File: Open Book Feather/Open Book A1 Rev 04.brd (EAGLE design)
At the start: 77.5 x 112.3 mm, 125 parts, among them J1 SJ-43514-SMT, J2 10118193-0001LF, Q1 DMG341, Q2 IRLML0100, SW1 SPDT_SWITCH, U1 AP2112-3.3, U2 MCP73831T-2ACI/OT, U3 ATSAMD51J64-TQFP(10X10), U4 GD25Q16C (or GD25Q32C), U5 74AC165D, U6 GD25Q16C (or GD25Q32C), U7 MAX4468EKAT, X1 JSTPH, X2 2x5 0.05" SWD

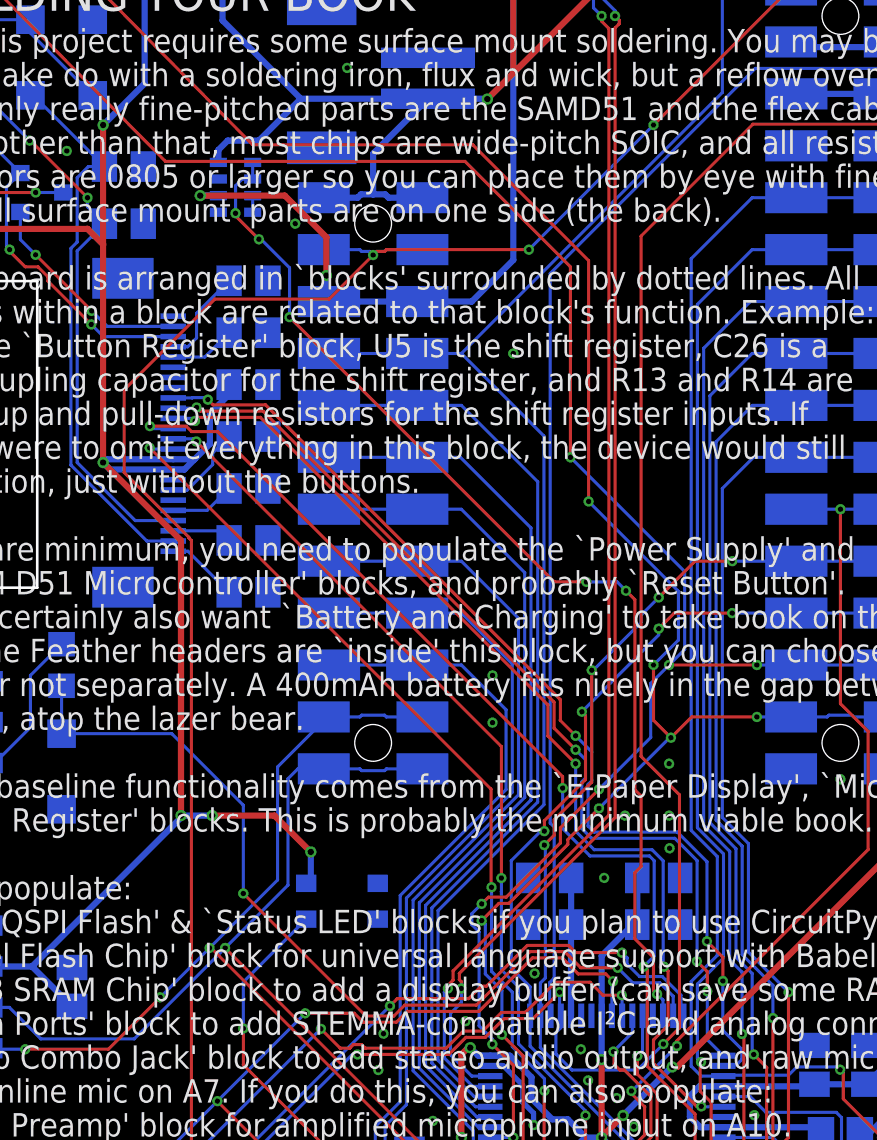
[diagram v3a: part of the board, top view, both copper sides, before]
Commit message: route A11/VBUSMON
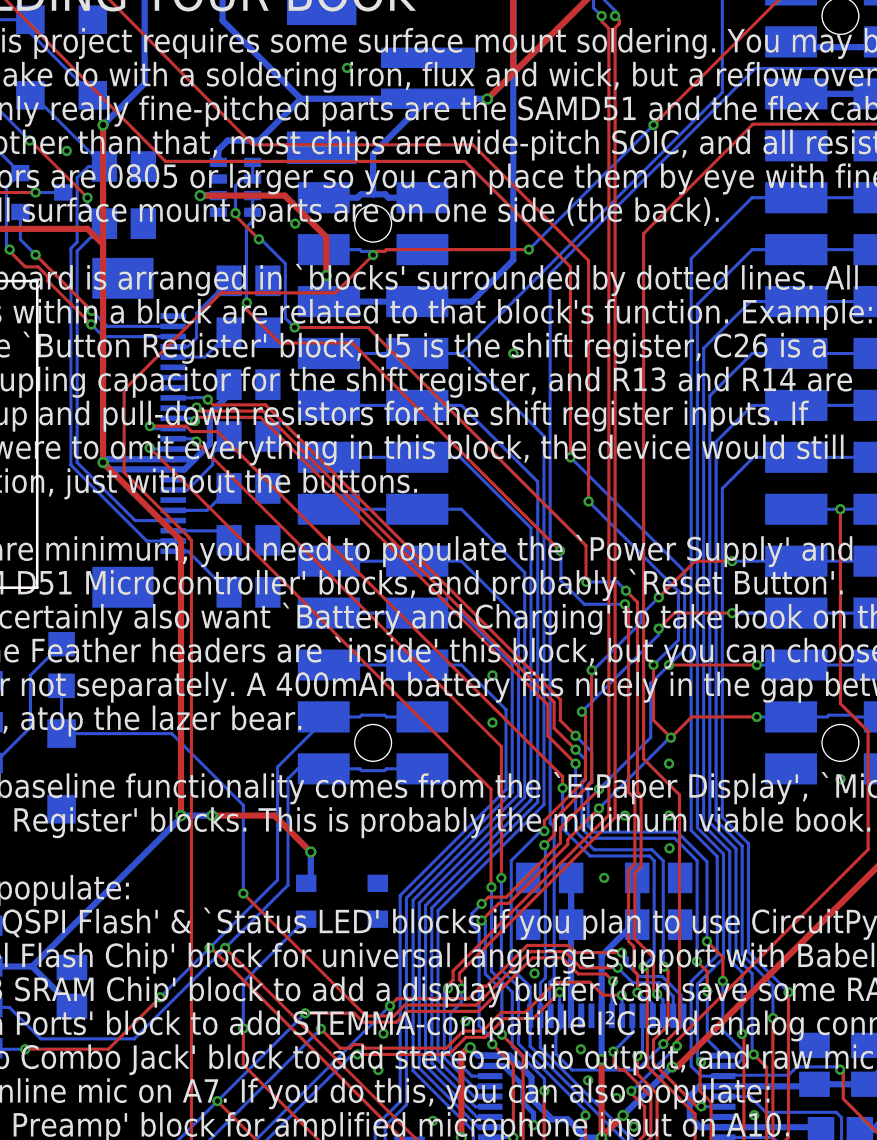
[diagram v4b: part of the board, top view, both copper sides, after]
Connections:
- net A11_BUSMON: now also U3.61
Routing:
- net A11_BUSMON: track 0.81 -> 52.1 mm, vias 0 -> 4
- net A6_BATMON: track 53.2 -> 54.3 mm
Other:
- board text added: "D1&Q1 conspire to let only the higher of VBAT & VBUS reach 3.3V regulator U1. C1 filters regulator input; C2 & C3 filter output. R1 pulls EN high to keep the regulator on. BATTERY: U2 is a LiPo charging controller. Powered by VBUS, it charges the battery at a rate determined by R3. C4=filter for VBAT, R4 limits current to CHG LED. R6: voltage dividers to gauge VBAT and VBUS on A6/PB01 and A11/PB0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"
- board text removed: "D1&Q1 conspire to let only the higher of VBAT & VBUS reach 3.3V regulator U1. C1 filters regulator input; C2 & C3 filter output. R1 pulls EN high to keep the regulator on. BATTERY: U2 is a LiPo charging controller. Powered by VBUS, it charges the battery at a rate determined by R3. C4=filter for VBAT, R4 limits current to CHG LED. R6: voltage dividers to gauge VBAT and VBUS on A6/PB01 and (TBD)."
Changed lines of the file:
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@@
      LED. R6: voltage dividers
      to gauge VBAT and VBUS
-     on A6/PB01 and (TBD).</text>
+     on A6/PB01 and A11/PB00.</text>
 <text x="32.004" y="95.758" size="0.6096" layer="22" font="vector" ratio="18" rot="MR270" align="center">VBAT</text>
 <text x="45.72" y="105.918" size="0.6096" layer="22" font="vector" ratio="18" rot="MR270" align="center">RESET</text>
@@
 <wire x1="15.255409375" y1="82.311409375" x2="18.415" y2="79.15181875" width="0.1524" layer="1"/>
 <wire x1="15.255409375" y1="86.364409375" x2="15.255409375" y2="82.311409375" width="0.1524" layer="1"/>
-<wire x1="19.6905" y1="90.7995" x2="15.255409375" y2="86.364409375" width="0.1524" layer="1"/>
+<wire x1="15.255409375" y1="86.364409375" x2="19.9953" y2="91.1043" width="0.1524" layer="1"/>
 <wire x1="55.306" y1="110.49" x2="55.052" y2="110.744" width="0.1524" layer="16"/>
 <wire x1="56.388" y1="109.8294" x2="55.7274" y2="110.49" width="0.1524" layer="16"/>
@@
 <wire x1="56.388" y1="109.8294" x2="56.388" y2="107.95" width="0.1524" layer="1"/>
 <wire x1="56.388" y1="107.95" x2="55.626" y2="107.188" width="0.1524" layer="1"/>
-<wire x1="25.2785" y1="90.7995" x2="19.6905" y2="90.7995" width="0.1524" layer="1"/>
-<wire x1="27.432" y1="92.953" x2="25.2785" y2="90.7995" width="0.1524" layer="1"/>
+<wire x1="25.5833" y1="91.1043" x2="19.9953" y2="91.1043" width="0.1524" layer="1"/>
+<wire x1="27.432" y1="92.953" x2="25.5833" y2="91.1043" width="0.1524" layer="1"/>
 </signal>
 <signal name="+3V3" class="1">
@@
 <wire x1="19.558" y1="40.429575" x2="9.9522125" y2="30.8237875" width="0.1524" layer="16"/>
 <wire x1="9.9522125" y1="30.8237875" x2="9.144" y2="31.632" width="0.1524" layer="16"/>
-<wire x1="46.013534375" y1="99.353534375" x2="40.5384" y2="93.8784" width="0.1524" layer="1"/>
-<wire x1="40.5384" y1="93.8784" x2="40.5384" y2="68.4276" width="0.1524" layer="1"/>
-<wire x1="40.5384" y1="68.4276" x2="42.418" y2="66.548" width="0.1524" layer="1"/>
+<wire x1="46.013534375" y1="99.353534375" x2="40.6654" y2="94.0054" width="0.1524" layer="1"/>
+<wire x1="40.6654" y1="94.0054" x2="40.6654" y2="68.3006" width="0.1524" layer="1"/>
+<wire x1="40.6654" y1="68.3006" x2="42.418" y2="66.548" width="0.1524" layer="1"/>
 <wire x1="36.3728" y1="53.8734" x2="36.3728" y2="54.9148" width="0.1524" layer="16"/>
 <wire x1="36.3728" y1="53.8734" x2="37.1602" y2="53.086" width="0.1524" layer="16"/>
@@
 <wire x1="39.8018" y1="76.5302" x2="39.37" y2="76.962" width="0.1524" layer="16"/>
 <via x="37.8646" y="76.962" extent="1-16" drill="0.254"/>
-<wire x1="37.8646" y1="76.962" x2="37.8553" y2="76.9713" width="0.1524" layer="1"/>
 <wire x1="41.148" y1="58.5945" x2="40.2336" y2="59.5089" width="0.1524" layer="1"/>
-<wire x1="39.8018" y1="76.5302" x2="40.2336" y2="76.0984" width="0.1524" layer="1"/>
-<wire x1="40.2336" y1="76.0984" x2="40.2336" y2="66.802" width="0.1524" layer="1"/>
+<wire x1="39.8018" y1="76.5302" x2="40.3606" y2="75.9714" width="0.1524" layer="1"/>
+<wire x1="40.3606" y1="75.9714" x2="40.3606" y2="66.675" width="0.1524" layer="1"/>
 <wire x1="40.2336" y1="62.738" x2="40.2336" y2="59.5089" width="0.1524" layer="1"/>
-<wire x1="40.2336" y1="66.802" x2="40.5384" y2="66.4972" width="0.1524" layer="1"/>
+<wire x1="40.3606" y1="66.675" x2="40.5384" y2="66.4972" width="0.1524" layer="1"/>
 <wire x1="40.5384" y1="63.0428" x2="40.2336" y2="62.738" width="0.1524" layer="1"/>
 <wire x1="40.5384" y1="66.4972" x2="40.5384" y2="63.0428" width="0.1524" layer="1"/>
-<wire x1="23.3426" y1="92.3306875" x2="23.3426" y2="89.916" width="0.1524" layer="16"/>
+<wire x1="23.1394" y1="92.5338875" x2="23.1394" y2="89.8652" width="0.1524" layer="16"/>
+<wire x1="23.5966" y1="89.408" x2="23.1394" y2="89.8652" width="0.1524" layer="16"/>
 <via x="20.701" y="94.996" extent="1-16" drill="0.254"/>
 <wire x1="20.701" y1="94.996" x2="20.701846875" y2="94.868153125" width="0.1524" layer="1"/>
@@
 <via x="21.844" y="93.726" extent="1-16" drill="0.254"/>
 <wire x1="21.844" y1="93.726" x2="21.9472875" y2="93.726" width="0.1524" layer="16"/>
-<wire x1="21.9472875" y1="93.726" x2="23.3426" y2="92.3306875" width="0.1524" layer="16"/>
+<wire x1="21.9472875" y1="93.726" x2="23.1394" y2="92.5338875" width="0.1524" layer="16"/>
 <wire x1="21.5392" y1="96.6724" x2="21.0312" y2="96.6724" width="0.1524" layer="16"/>
 <wire x1="21.0312" y1="96.6724" x2="20.701" y2="96.3422" width="0.1524" layer="16"/>
 <wire x1="20.701" y1="96.3422" x2="20.701" y2="94.996" width="0.1524" layer="16"/>
-<wire x1="37.8553" y1="76.9713" x2="36.2873" y2="76.9713" width="0.1524" layer="1"/>
-<wire x1="36.2873" y1="76.9713" x2="23.3426" y2="89.916" width="0.1524" layer="1"/>
-<via x="23.3426" y="89.916" extent="1-16" drill="0.254"/>
+<via x="23.5966" y="89.408" extent="1-16" drill="0.254"/>
 <contactref element="R6" pad="1"/>
 <wire x1="21.5392" y1="96.6724" x2="21.5392" y2="97.4852" width="0.1524" layer="16"/>
+<wire x1="37.846" y1="76.9806" x2="37.846" y2="78.74" width="0.1524" layer="1"/>
+<wire x1="37.846" y1="78.74" x2="27.178" y2="89.408" width="0.1524" layer="1"/>
+<wire x1="27.178" y1="89.408" x2="23.5966" y2="89.408" width="0.1524" layer="1"/>
+<wire x1="37.8646" y1="76.962" x2="37.846" y2="76.9806" width="0.1524" layer="1"/>
 </signal>
 <signal name="A11_BUSMON">
@@
 <contactref element="R6" pad="3"/>
 <wire x1="21.5392" y1="95.0468" x2="21.5392" y2="95.8596" width="0.1524" layer="16"/>
+<contactref element="U3" pad="61"/>
+<via x="40.3606" y="56.8706" extent="1-16" drill="0.254"/>
+<wire x1="40.8566875" y1="56.5666" x2="40.6646" y2="56.5666" width="0.1524" layer="16"/>
+<wire x1="40.6646" y1="56.5666" x2="40.3606" y2="56.8706" width="0.1524" layer="16"/>
+<wire x1="41.112" y1="55.738" x2="41.112" y2="56.3112875" width="0.1524" layer="16"/>
+<wire x1="41.112" y1="56.3112875" x2="40.8566875" y2="56.5666" width="0.1524" layer="16"/>
+<wire x1="40.3606" y1="56.8706" x2="40.3606" y2="57.7629" width="0.1524" layer="1"/>
+<wire x1="40.3606" y1="57.7629" x2="40.1828" y2="57.9407" width="0.1524" layer="1"/>
+<wire x1="40.2336" y1="63.16905625" x2="40.2336" y2="66.37094375" width="0.1524" layer="1"/>
+<wire x1="40.2336" y1="66.37094375" x2="39.9288" y2="66.67574375" width="0.1524" layer="1"/>
+<wire x1="39.9288" y1="59.38264375" x2="39.9288" y2="62.86425625" width="0.1524" layer="1"/>
+<wire x1="39.9288" y1="62.86425625" x2="40.2336" y2="63.16905625" width="0.1524" layer="1"/>
+<wire x1="40.1828" y1="59.12864375" x2="39.9288" y2="59.38264375" width="0.1524" layer="1"/>
+<wire x1="40.1828" y1="57.9407" x2="40.1828" y2="59.12864375" width="0.1524" layer="1"/>
+<wire x1="39.9288" y1="75.692" x2="39.751" y2="75.8698" width="0.1524" layer="1"/>
+<via x="39.751" y="75.8698" extent="1-16" drill="0.254"/>
+<via x="36.576" y="78.486" extent="1-16" drill="0.254"/>
+<wire x1="36.62" y1="78.442" x2="36.576" y2="78.486" width="0.1524" layer="16"/>
+<wire x1="36.62" y1="77.0161" x2="36.62" y2="78.442" width="0.1524" layer="16"/>
+<wire x1="37.7663" y1="75.8698" x2="36.62" y2="77.0161" width="0.1524" layer="16"/>
+<wire x1="39.751" y1="75.8698" x2="37.7663" y2="75.8698" width="0.1524" layer="16"/>
+<wire x1="21.2586125" y1="90.6217" x2="21.2344" y2="90.6459125" width="0.1524" layer="16"/>
+<wire x1="21.2344" y1="94.3069" x2="21.5392" y2="94.6117" width="0.1524" layer="16"/>
+<wire x1="21.5392" y1="94.6117" x2="21.5392" y2="95.0468" width="0.1524" layer="16"/>
+<wire x1="21.2344" y1="90.6459125" x2="21.2344" y2="94.3069" width="0.1524" layer="16"/>
+<wire x1="39.9288" y1="66.67574375" x2="39.9288" y2="75.692" width="0.1524" layer="1"/>
+<wire x1="36.576" y1="78.486" x2="26.416" y2="88.646" width="0.1524" layer="1"/>
+<wire x1="26.416" y1="88.646" x2="22.8787125" y2="88.646" width="0.1524" layer="1"/>
+<wire x1="22.8787125" y1="88.646" x2="21.2586125" y2="90.2661" width="0.1524" layer="1"/>
+<wire x1="21.2586125" y1="90.2661" x2="21.2586125" y2="90.6217" width="0.1524" layer="1"/>
+<via x="21.2586125" y="90.6217" extent="1-16" drill="0.254"/>
 </signal>
 <signal name="MIC_BIAS_PWR">

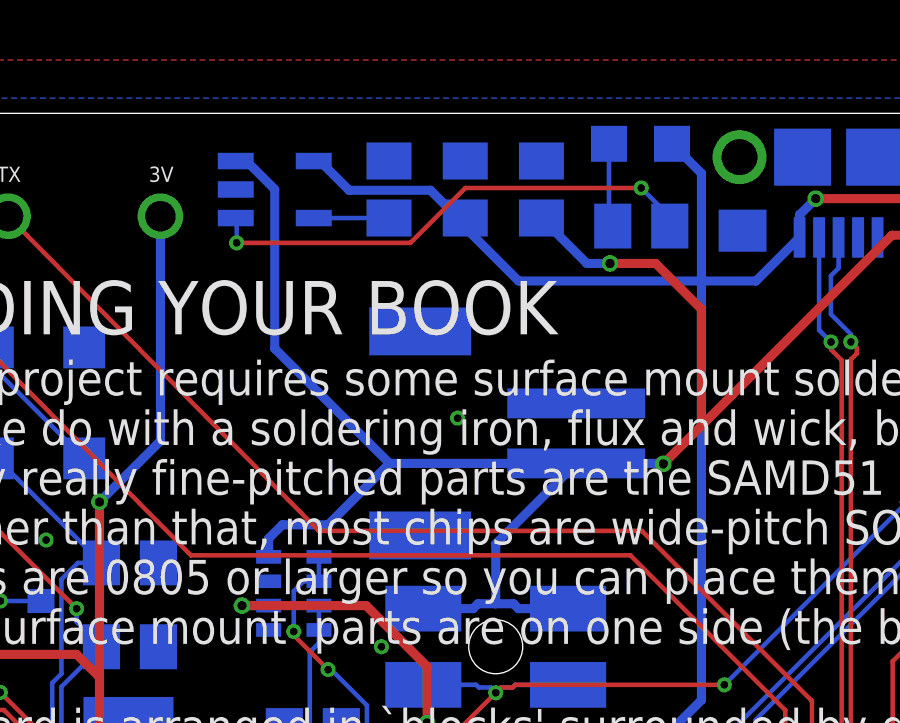
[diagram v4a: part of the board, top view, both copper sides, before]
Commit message: add green led for full battery
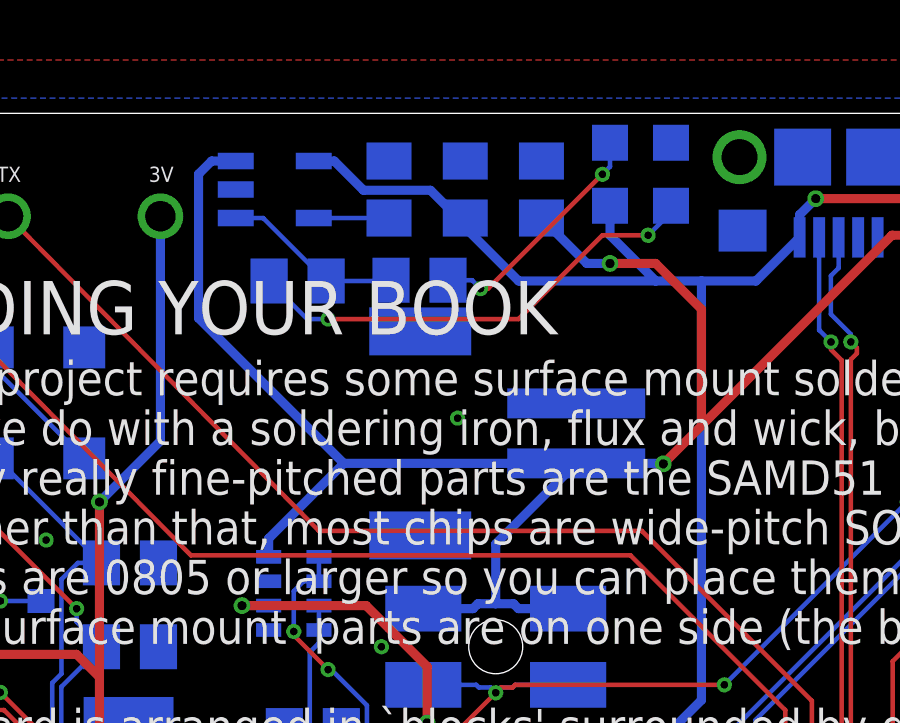
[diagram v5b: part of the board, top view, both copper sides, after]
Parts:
- added FUL: GREEN, adafruit:CHIP-LED0805
- added R5: 1K, microbuilder:0805-NO
- moved R4 7.61 mm to (24.9, 106.7), turned to 0 degrees
- moved CHG 1.44 mm to (31.2, 110.2), turned to 0 degrees
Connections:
- removed net N$5: R4.2, U2.1
- new net N$9: FUL.A, R5.1
- new net STAT: R4.2, R5.2, U2.1
- net GND: now also FUL.C
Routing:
- net N$5: track 16.7 -> 0.00 mm, vias 2 -> 0
- net N$9: track 0.00 -> 15.6 mm, vias 0 -> 2
- net STAT: track 0.00 -> 6.06 mm
- net N$4: track 2.80 -> 8.00 mm, vias 0 -> 2
- net VBUS: track 76.5 -> 74.6 mm
- net VBAT: track 68.4 -> 69.1 mm
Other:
- board text added: "D1&Q1 conspire to let only the higher of VBAT & VBUS reach 3.3V regulator U1. C1 filters regulator input; C2 & C3 filter output. R1 pulls EN high to keep the regulator on. BATTERY: U2 is a LiPo charging controller. Powered by VBUS, it charges the battery at a rate determined by R3. C4=filter for VBAT, R4&R5 limit current to CHG & FUL LEDs. R6: voltage dividers to gauge VBAT and VBUS on A6/PB01 an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"
- board text added: "Notes at end of the POWER SUPPLY block."
- board text removed: "*See notes on this bit at bottom of the POWER SUPPLY block."
- board text removed: "D1&Q1 conspire to let only the higher of VBAT & VBUS reach 3.3V regulator U1. C1 filters regulator input; C2 & C3 filter output. R1 pulls EN high to keep the regulator on. BATTERY: U2 is a LiPo charging controller. Powered by VBUS, it charges the battery at a rate determined by R3. C4=filter for VBAT, R4 limits current to CHG LED. R6: voltage dividers to gauge VBAT and VBUS on A6/PB01 and A11/PB0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"
